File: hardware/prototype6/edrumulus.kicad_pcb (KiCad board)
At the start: 2 copper layers, 106 parts, among them J1 Hi-Hat, J10 DIN-5, J11 DIN-5, J2 Snare, J3 Crash, J4 Ride, J5 Tom1, J6 Tom2, J7 Tom3, J8 Kick, J9 Hi-Hat-Ctrl, U1 ESP32-DEVKIT-V1, U2 6N138, U3 MCP1754S-3302xMB

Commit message: more work on prototype 6
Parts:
- J10: value DIN-5 -> MIDI-IN
- J11: value DIN-5 -> MIDI-OUT
- moved C34 230.0 mm to (297.2, -46.4)
- moved C33 186.9 mm to (288.3, -14.0)
- moved C35 179.7 mm to (287.7, -26.7)
- moved D21 177.0 mm to (35.6, 66.0)
- moved C36 172.9 mm to (274.4, -46.4)
- moved C11 170.4 mm to (275.8, -32.4)
- moved U3 168.8 mm to (263.8, -43.8)
- moved D1 166.9 mm to (55.2, 76.8)
- moved C37 163.5 mm to (273.1, -41.3)
- moved C12 158.5 mm to (98.7, 105.2), turned to 180 degrees
- moved C31 156.6 mm to (285.8, -45.7)
- moved C32 156.6 mm to (285.8, -33.6)
- moved R19 152.9 mm to (68.6, 111.7)
- moved R35 151.9 mm to (68.6, 105.3)
- moved R21 149.5 mm to (68.6, 127.6)
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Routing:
- net GND: track 0.00 -> 41.7 mm
- net GPIO13: track 0.00 -> 4.16 mm
- net GPIO12: track 0.00 -> 3.89 mm
- net GPIO33: track 0.00 -> 3.83 mm
- net GPIO36: track 0.00 -> 3.75 mm
- net GPIO14: track 0.00 -> 3.61 mm
- net GPIO32: track 0.00 -> 3.55 mm
- net GPIO39: track 0.00 -> 3.47 mm
- net GPIO27: track 0.00 -> 3.33 mm
- net GPIO35: track 0.00 -> 3.27 mm
- net GPIO34: track 0.00 -> 3.19 mm
- net GPIO26: track 0.00 -> 3.13 mm
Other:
- board outline added: 201.3 x 115.6 mm

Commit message: more component placement for prototype 6
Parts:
- moved U3 274.8 mm to (39.7, 115.3), turned to 90 degrees
- moved C33 274.4 mm to (48.8, 119.8), turned to 90 degrees
- moved C38 263.3 mm to (42.6, 126.0), turned to 180 degrees
- moved C34 261.7 mm to (71.3, 85.6), turned to 180 degrees
- moved C11 261.1 mm to (46.1, 91.7), turned to 90 degrees
- moved C8 256.5 mm to (46.7, 101.8), turned to 90 degrees
- moved C31 254.9 mm to (71.4, 92.1), turned to 180 degrees
- moved C36 249.5 mm to (71.3, 98.5), turned to 180 degrees
- moved C32 239.6 mm to (71.2, 73.1), turned to 180 degrees
- moved C37 234.9 mm to (71.4, 79.1), turned to 180 degrees
- moved C35 185.0 mm to (156.9, 104.1), turned to 180 degrees
- moved R23 141.4 mm to (73.7, 103.5)
- moved R15 129.6 mm to (86.2, 103.5)
- moved R43 107.5 mm to (181.4, 84.8), turned to -90 degrees
- moved R40 85.0 mm to (186.9, 84.3), turned to 0 degrees
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
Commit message: use different regulator for prototype 6
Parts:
- removed C38: 100n, Capacitor_THT:C_Disc_D5.0mm_W2.5mm_P5.00mm
- added C15: 100n, Capacitor_THT:C_Disc_D5.0mm_W2.5mm_P5.00mm, F.Cu at (103.7, 107.4)
- U3: value MCP1754S-3302xMB -> L78L33_TO92; footprint Package_TO_SOT_SMD:SOT-89-3 -> Package_TO_SOT_THT:TO-92_Inline
- moved C33 36.5 mm to (82.8, 106.8), turned to 0 degrees
- moved C11 31.6 mm to (72.4, 109.1), turned to 180 degrees
- moved U3 30.5 mm to (67.3, 102.3), turned to 180 degrees
- moved C8 12.2 mm to (58.9, 102.2)
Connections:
- U3 pad 1: 5V -> 3V3
- U3 pad 3: 3V3 -> 5V

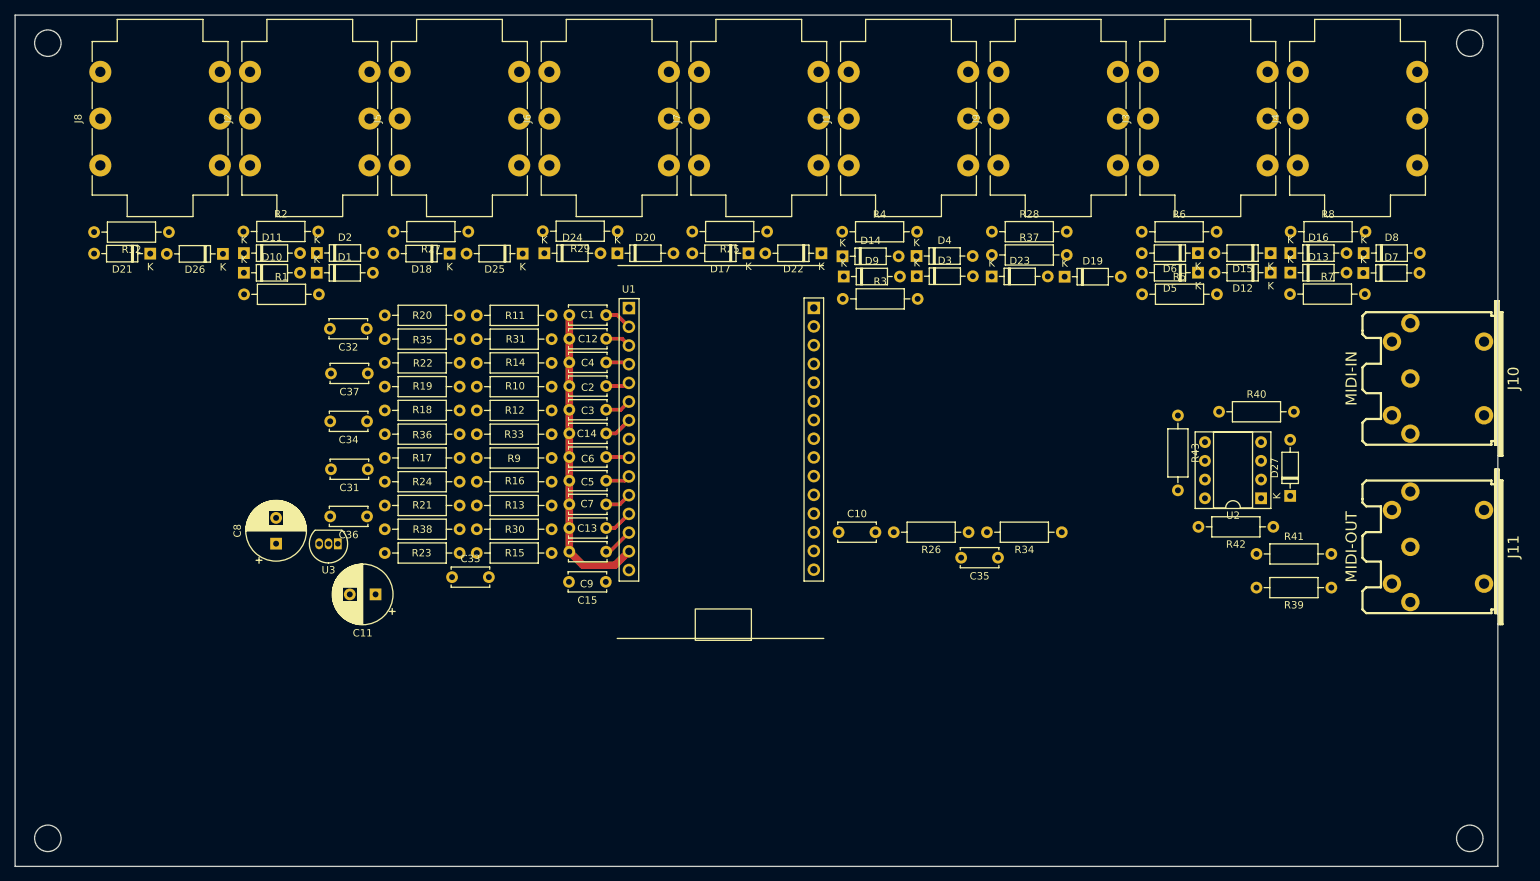
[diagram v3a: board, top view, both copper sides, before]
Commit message: finished placement of components of prototype 6
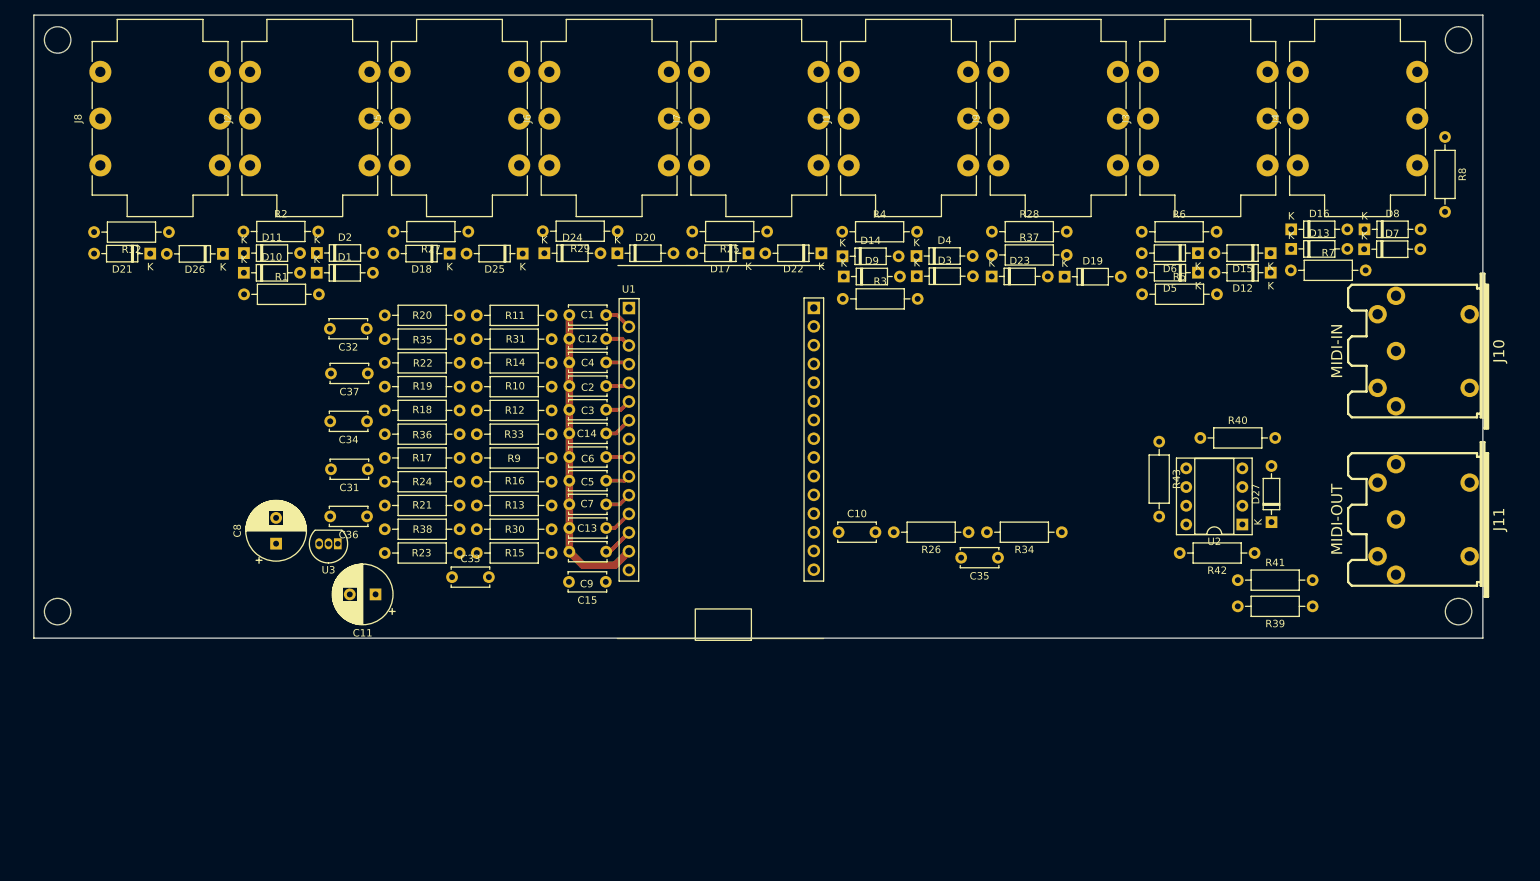
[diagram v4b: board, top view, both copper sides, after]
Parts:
- moved R8 24.6 mm to (217.6, 47.0), turned to -90 degrees
- moved U2 4.37 mm to (190.1, 99.6)
- moved D27 4.37 mm to (194.1, 99.3)
- moved R40 4.37 mm to (184.4, 87.9)
- moved R41 4.37 mm to (189.5, 107.2)
- moved R42 4.37 mm to (191.8, 103.5)
- moved R43 4.37 mm to (178.8, 88.4)
- moved J10 4.20 mm to (214.0, 76.1)
- moved J11 4.20 mm to (214.0, 98.9)
- moved R39 3.59 mm to (199.6, 110.7)
- moved D13 3.23 mm to (196.7, 62.2)
- moved D16 3.23 mm to (196.7, 59.6)
- moved D7 3.23 mm to (206.6, 62.3)
- moved D8 3.23 mm to (206.7, 59.6)
- moved R7 3.23 mm to (196.7, 65.1)
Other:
- board size 201.3 x 115.6 mm -> 196.7 x 84.6 mm
